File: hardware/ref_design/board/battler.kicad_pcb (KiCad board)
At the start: 2 copper layers, 71.4 x 151.2 mm, 173 parts, among them J1 TYPE-C-31-M-12, J2 53261-0271, J3 FH12-50S-0.5SH(55), J4 SPEAKER, J5 SWD, J6 UART, J7 DEBUG PADS, Q1 2N7002, Q2 AO3401A, Q3 2N7002, Q4 2N7002, Q5 AO3400A, Q6 AO3400A, SW1 P1 UP, SW10 P2 DOWN, SW11 P2 LEFT, SW12 P2 RIGHT, SW13 P2 A, SW14 P2 B, SW15 P2 X, SW16 P2 Y, SW18 BOOTSEL, SW19 RESET, SW2 P1 DOWN, SW20 P1 SELECT, SW21 P1 START / PWR, SW22 P2 SELECT, SW23 P2 START, SW3 P1 LEFT, SW4 P1 RIGHT, SW5 P1 A, SW6 P1 B, SW7 P1 X, SW8 P1 Y, SW9 P2 UP, U1 SRV05-4, U2 TP4056-42-ESOP8, U3 ME6211C33M5G, U4 RP2354B, U6 MCP6002, U7 FM8002A, X1 12MHz

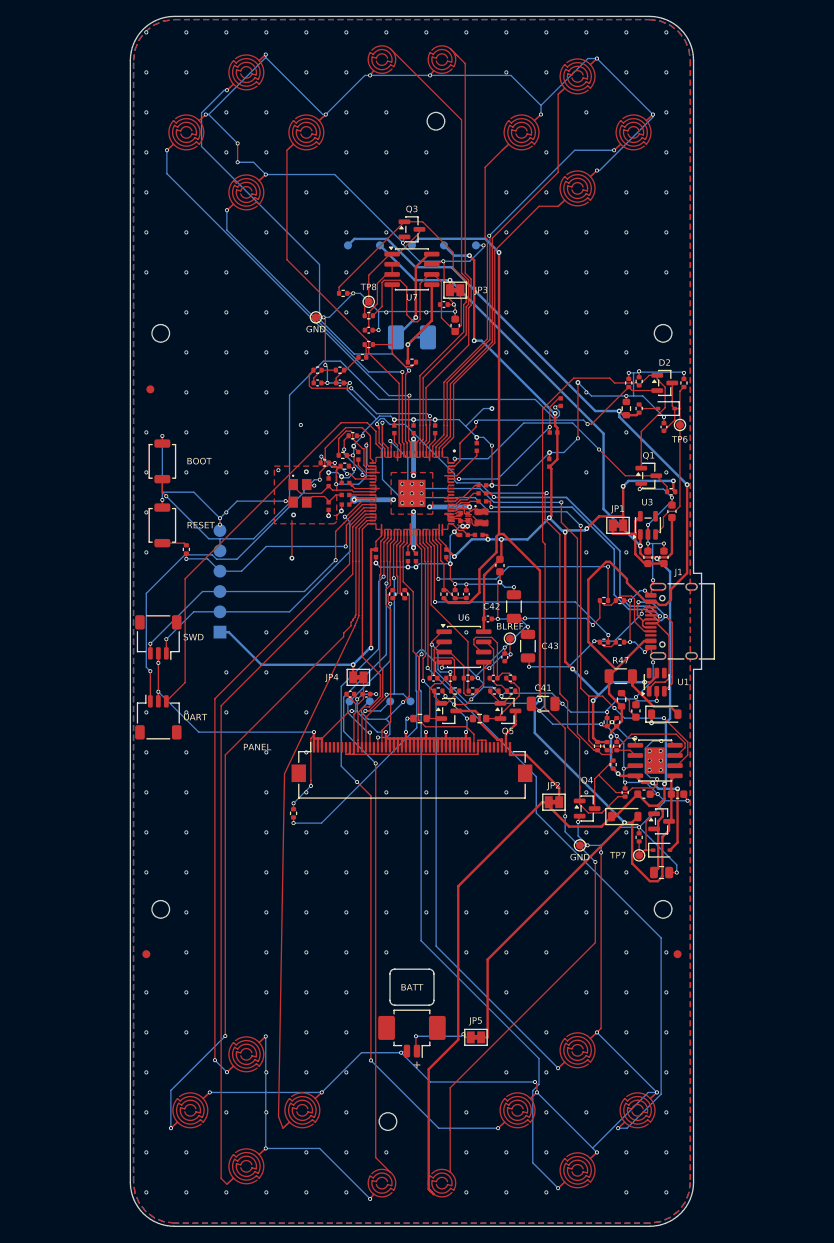
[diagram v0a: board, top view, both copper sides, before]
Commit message: ref_design board: rebuilt for the moved battery plug hole
build_pcb from the merged schematic (no-connect pads on their unconnected nets) with the
plug hole from positions.json, routed with route.py 80 (the fourth of six attempts; the
others left one connection open, mostly J1's shield leg or a seat-1 line), silk, fab.
check_pcb: 0 unconnected, 0 parity, the 4 known silk warnings. check_fit passes.

Co-Authored-By: Claude Opus 5.5 <noreply@anthropic.com>
Claude-Session: https://claude.ai/code/session_01NxPKqL46d94oRzrtCbFjri
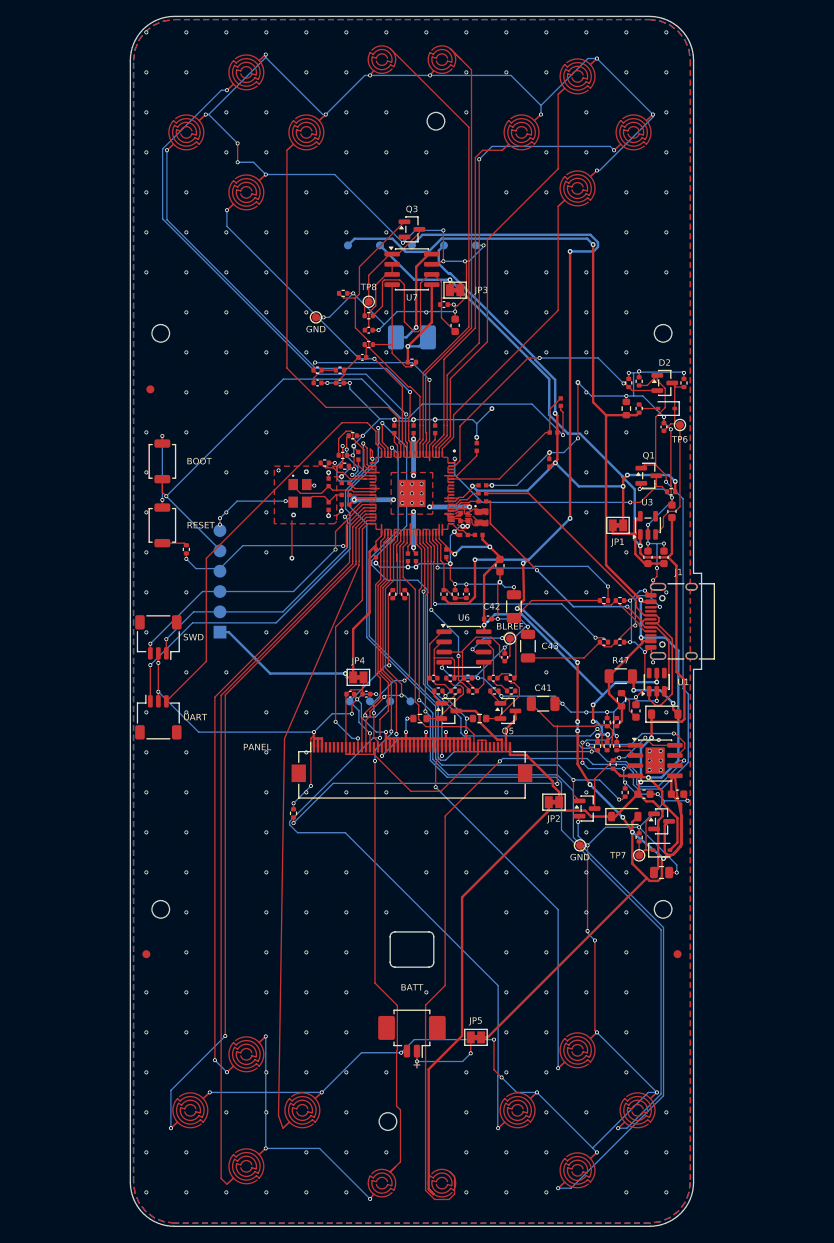
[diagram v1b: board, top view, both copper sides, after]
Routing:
- net VBAT: track 164.3 -> 201.1 mm, vias 3 -> 12
- net P1_B: track 91.3 -> 110.5 mm
- net PWR_BTN_RAW: track 135.9 -> 149.3 mm
- net USB_DM: track 52.3 -> 39.9 mm, vias 3 -> 2
- net AMP_EN: track 48.5 -> 37.5 mm
- net /USB_Charger/CHG_CE: track 25.4 -> 16.3 mm
- net /USB_Charger/CHG_TEMP: track 69.2 -> 60.9 mm, vias 5 -> 2
- net P1_A: track 90.8 -> 99.0 mm
- net P2_LEFT: track 51.3 -> 57.9 mm
- net P1_Y: track 90.5 -> 96.5 mm, vias 4 -> 2
- net CHG_DONE_N: track 88.1 -> 93.9 mm, vias 4 -> 3
- net CHG_STAT_N: track 76.6 -> 82.3 mm, vias 2 -> 4
- net VBUS: track 139.0 -> 144.7 mm, vias 6 -> 4
- net UART_RX: track 56.7 -> 51.6 mm
- net P2_B: track 61.9 -> 66.6 mm
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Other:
- outline, holes or cut-outs redrawn

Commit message: ref_design board: rebuilt for U1, J4 and its hole; the router grounds J1's shell legs
route.py: usb_shell_ground() joins J1's front and rear shell legs on the back and gives each
a via (the routing used to cut their patch of pour off: 5 runs in 6 failed there), keeps
vias and routes out of both plug holes, and the maze finish can rip up one other net's copper
anywhere along a long connection (corridor_ripup). Routing passed 5 runs in 6 (2/3, then 3/3);
J1 never failed again. silk.py keeps labels off the plug holes.

check_pcb PASS (0 unconnected, 0 parity, the 4 known silk warnings); fab; check_fit PASS.
cost.py: 49 parts (11 extended, from 12), $4.73 a board, $33 setup an order (from $36).
Docs: assembly (no soldering), bom, design_review, README, PLAN.

Co-Authored-By: Claude Opus 5.5 <noreply@anthropic.com>
Claude-Session: https://claude.ai/code/session_01NxPKqL46d94oRzrtCbFjri
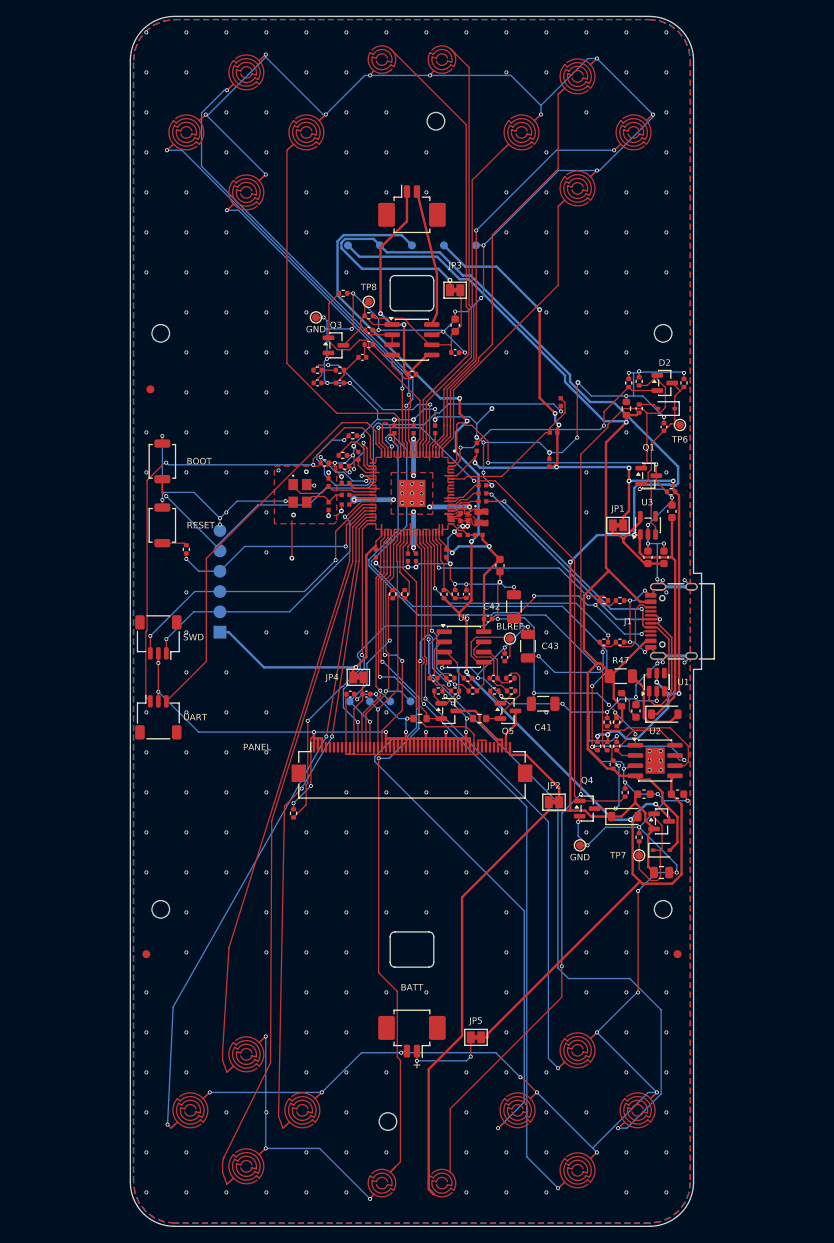
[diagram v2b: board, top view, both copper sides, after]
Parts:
- J4: value SPEAKER -> 53261-0271; footprint battler:Speaker_Wire_Pads_P4.0mm -> Connector_Molex:Molex_PicoBlade_53261-0271_1x02-1MP_P1.25mm_Horizontal; moved to F.Cu
- moved Q3 17.3 mm to (90.5, 65.5)
- moved J4 15.8 mm to (100.0, 48.7), turned to 0 degrees
- moved U7 8.80 mm to (100.0, 64.8)
- moved C35 6.16 mm to (105.4, 66.4)
- moved R35 1.50 mm to (100.0, 69.1)
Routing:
- net VSYS: track 183.7 -> 238.8 mm, vias 4 -> 3
- net VBAT: track 201.1 -> 169.2 mm, vias 12 -> 6
- net PWR_BTN_RAW: track 149.3 -> 125.0 mm
- net P1_B: track 110.5 -> 90.7 mm
- net GND: track 763.8 -> 783.6 mm, vias 366 -> 352
- net /USB_Charger/CHG_TEMP: track 60.9 -> 78.1 mm, vias 2 -> 5
- net /Audio/SPK_P: track 13.9 -> 30.5 mm, vias 1 -> 2
- net /Audio/AMP_VDD: track 34.8 -> 19.7 mm
- net /Display/BL_S2: track 9.65 -> 21.5 mm, vias 0 -> 2
- net UART_RX: track 51.6 -> 63.1 mm
- net VBUS: track 144.7 -> 135.1 mm, vias 4 -> 1
- net /Display/BL_FB1: track 16.0 -> 6.99 mm, vias 2 -> 0
- net /MCU/REV2: track 8.61 -> 17.3 mm
- net CHG_DONE_N: track 93.9 -> 85.3 mm, vias 3 -> 2
- net CHG_OFF: track 80.1 -> 71.6 mm, vias 3 -> 2
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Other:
- outline, holes or cut-outs redrawn

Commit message: ref_design board: re-placed and re-routed for the 133 mm shell
70.4 x 127.7 to case/BOARD_OUTLINE.md: charger and power latch round the
moved screws, the backlight sinks right of the core, the amplifier in the
left bezel's seat-2 corner, the core 2.5 mm towards seat 1 so its top
pins fan out below the speaker plug's hole, JP5 clear of the cluster, TH1
over the cell clear of the FPC. J2 and J4 stay at the ends under the
spines. Back silkscreen outlines the cell and the speaker. check_fit 0,
DRC 0 errors and 0 unrouted, ERC 0.

Co-Authored-By: Claude Opus 5.5 <noreply@anthropic.com>
Claude-Session: https://claude.ai/code/session_01Y3mFMxLYqNeyyedvbYuRwX
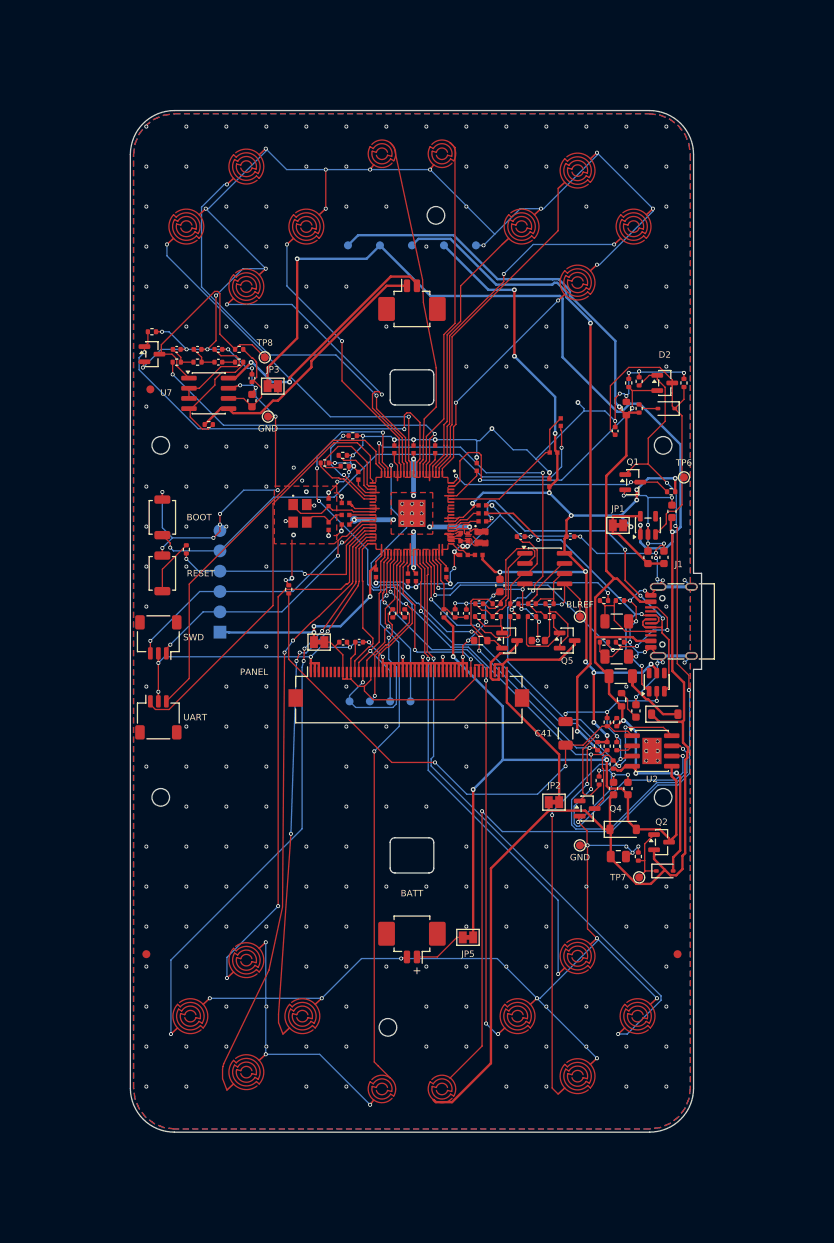
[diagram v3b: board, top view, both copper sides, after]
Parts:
- R61: value 3.9k -> 2.4k
- moved TH1 28.0 mm to (84.6, 96.0)
- moved C34 27.1 mm to (80.0, 72.4)
- moved U7 26.3 mm to (74.6, 71.5)
- moved R35 26.2 mm to (74.6, 75.4)
- moved JP3 25.8 mm to (82.6, 70.6)
- moved C35 25.6 mm to (80.0, 69.6), turned to 90 degrees
- moved R37 24.4 mm to (67.5, 63.8)
- moved Q3 23.0 mm to (67.5, 66.6)
- moved C40 19.0 mm to (75.8, 66.0)
- moved C38 18.3 mm to (73.2, 66.0)
- moved C37 18.1 mm to (70.6, 66.0)
- moved C39 18.0 mm to (75.8, 67.6)
- moved R33 17.8 mm to (73.2, 67.6)
- moved R32 17.6 mm to (70.6, 67.6)
- moved R36 16.7 mm to (78.4, 66.0)
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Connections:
- J3 pad 14: LCD_DC -> /Display/LCD_SCK
- J3 pad 15: /Display/LCD_SCK -> LCD_DC
- J3 pad 45: unconnected-(J3-Pin_45-Pad45) -> GND
- J3 pad 46: unconnected-(J3-Pin_46-Pad46) -> /Display/LED_K2
- J3 pad 47: unconnected-(J3-Pin_47-Pad47) -> /Display/LED_K1
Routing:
- net GND: track 783.6 -> 703.8 mm, vias 352 -> 303
- net AMP_EN: track 29.5 -> 52.4 mm, vias 0 -> 2
- net P1_Y: track 91.3 -> 70.2 mm, vias 2 -> 4
- net AUDIO_PWM: track 23.8 -> 42.8 mm
- net P1_SELECT: track 87.9 -> 69.4 mm
- net /Audio/AMP_SHDN: track 10.6 -> 29.2 mm
- net P1_A: track 95.2 -> 76.8 mm
- net /Power/PWR_EN: track 23.1 -> 41.4 mm
- net CHG_DONE_N: track 85.3 -> 103.5 mm, vias 2 -> 6
- net +3V3: track 214.2 -> 198.7 mm, vias 15 -> 20
- net /Audio/SPK_N: track 17.1 -> 31.8 mm, vias 0 -> 2
- net P1_X: track 75.4 -> 61.0 mm
- net P2_START: track 57.3 -> 42.9 mm
- net P2_Y: track 49.2 -> 35.7 mm, vias 0 -> 2
- net P1_RIGHT: track 80.5 -> 67.3 mm, vias 2 -> 4
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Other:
- board size 71.4 x 151.2 mm -> 71.4 x 127.7 mm
- board text added: "CELL"
- board text added: "SPK PLUG"

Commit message: WIP: cell and speaker holes, core on the back (unrouted)
Co-Authored-By: Claude Opus 5.5 <noreply@anthropic.com>
Claude-Session: https://claude.ai/code/session_01Y3mFMxLYqNeyyedvbYuRwX
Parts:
- C1, C10, C11, C12, C13, C14, C15, C16, C17, C18, C19, C20, C21, C22, C23, C24, C25, C26, C27, C28, C29, C30, C47, C48, C49, C5, C50, C51, C6, C7, C8, JP4, L2, R1, R13, R14, R15, R16, R17, R18, R19, R2, R20, R21, R22, R23, R25, R28, R29, R3, R38, R4, R41, R42, R47, R48, R49, R50, R51, R52, R53, R54, R55, R56, R57, R58, R59, R60, R61, TP10, TP6, U4, X1: moved to B.Cu
- TP9: moved to F.Cu
- moved R37 79.1 mm to (92.0, 139.0)
- moved Q1 78.4 mm to (68.6, 134.2)
- moved D3 76.5 mm to (80.6, 130.2), turned to 0 degrees
- moved JP3 75.7 mm to (104.0, 143.2)
- moved C35 74.3 mm to (105.0, 139.6)
- moved C40 72.1 mm to (93.0, 136.0), turned to 90 degrees
- moved C34 71.8 mm to (103.6, 140.2)
- moved R15 71.7 mm to (109.6, 137.6), turned to 180 degrees
- moved R36 71.3 mm to (91.8, 136.0), turned to 90 degrees
- moved R34 70.5 mm to (95.4, 136.0), turned to 90 degrees
- moved C37 70.3 mm to (91.8, 133.0), turned to 90 degrees
- moved C38 70.2 mm to (94.2, 133.0), turned to 90 degrees
- moved Q3 69.9 mm to (88.0, 133.4)
- moved U7 69.7 mm to (100.0, 136.4), turned to 90 degrees
- moved R38 69.2 mm to (110.4, 140.6), turned to 180 degrees
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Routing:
- net GND: track 703.8 -> 12.9 mm, vias 303 -> 22
- net VSYS: track 228.3 -> 0.00 mm, vias 3 -> 0
- net VBAT: track 168.8 -> 0.00 mm, vias 5 -> 0
- net +3V3: track 198.7 -> 37.8 mm, vias 20 -> 0
- net VBUS: track 136.5 -> 0.00 mm, vias 4 -> 0
- net PWR_BTN_RAW: track 125.1 -> 0.00 mm, vias 4 -> 0
- net CHG_DONE_N: track 103.5 -> 3.89 mm, vias 6 -> 0
- net CHG_STAT_N: track 89.9 -> 3.89 mm, vias 6 -> 0
- net P1_B: track 86.1 -> 3.85 mm, vias 2 -> 0
- net CHG_OFF: track 79.1 -> 3.89 mm, vias 4 -> 0
- net P1_A: track 76.8 -> 3.85 mm, vias 2 -> 0
- net P1_DOWN: track 77.2 -> 7.46 mm, vias 2 -> 0
- net P1_LEFT: track 73.6 -> 6.84 mm, vias 4 -> 0
- net P1_Y: track 70.2 -> 3.81 mm, vias 4 -> 0
- net P1_SELECT: track 69.4 -> 3.81 mm, vias 2 -> 0
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- added copper zone on B.Cu, net +1V1
- added copper zone on B.Cu, net +3V3
- added copper zone on B.Cu, net VREG_LX
- removed copper zone on F.Cu, net +1V1
- removed copper zone on F.Cu, net +3V3
- removed copper zone on F.Cu, net GND
- removed copper zone on F.Cu, net VREG_LX
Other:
- outline, holes or cut-outs redrawn
- board text removed: "+"
- board text removed: "1V1"
- board text removed: "2 LAYERS 1.6 MM ENIG"
- board text removed: "3V3"
- board text removed: "BATT"
- board text removed: "BLREF"
- board text removed: "BOOT"
- board text removed: "CELL"
- board text removed: "CS"
- board text removed: "DC"
- board text removed: "GND"
- board text removed: "MOSI"
- board text removed: "PANEL"
- board text removed: "RESET"
- board text removed: "REV 1"
- board text removed: "SCK"
- board text removed: "SPEAKER"
- board text removed: "SPK PLUG"
- board text removed: "SWD"
- board text removed: "SWD PADS"
- board text removed: "TWO-PLAYER HANDHELD REF-A"
- board text removed: "UART"
- board text removed: "VBAT"
- board text removed: "VBUS"
- board text removed: "VSYS"
